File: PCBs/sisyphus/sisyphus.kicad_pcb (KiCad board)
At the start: 2 copper layers, 52 x 42 mm, 68 parts, among them J1 USB_BOOT, J10 Speaker, J2 SWD, J3 Battery, J4 USB_C_Receptacle_USB2.0_14P, J5 Keyboard, J6 AUX USB, J7 Light sensor, J8 Limit SW, J9 RGB_CONN, Q1 AO3401A, SW1 SW_SPDT_321, U1 W25Q128JVS, U2 RP2040, U3 TPS62291, U4 BQ25619, U5 USBLC6-2P6, U6 TCA8418, U7 MAX98357A, Y1 ABM8-272-T3

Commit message: Schematic refinements, start of PCB
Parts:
- removed C25: 10uF, Capacitor_SMD:C_0402_1005Metric
- removed D2: D_shottky, Diode_SMD:D_SOD-123
- removed J10: Speaker, Connector_PinHeader_2.54mm:PinHeader_1x02_P2.54mm_Vertical
- removed L2: 2.2uH 1.2A, Inductor_SMD:L_0805_2012Metric
- removed R14: DNF, Resistor_SMD:R_0402_1005Metric
- added JP2: Gain select, Jumper:SolderJumper-3_P1.3mm_Open_RoundedPad1.0x1.5mm, B.Cu at (112.5, 97.0)
- added U8: RP2040, Package_DFN_QFN:QFN-56-1EP_7x7mm_P0.4mm_EP3.2x3.2mm, F.Cu at (102.3, 95.0)
- C1: value 100nF -> 1uF
- C11, C12: value 1uF -> 100nF
- C13, C17, C20: value 10uF -> 100nF
- C14, C15: value 15pF -> 100nF
- C16: value 47nF -> 100nF
- C19: value 10uF -> 1uF
- C2, C24, C3, C7: value 100nF -> 10uF
- C22: value 4.7uF -> 15pF
- C23: value 10uF -> 15pF
- C4: value 100nF -> 0.1uF
- C5: value 100nF -> 4.7uF
- D1: value LED -> D_shottky; footprint LED_SMD:LED_0603_1608Metric -> Diode_SMD:D_SOD-123
- J1: value USB_BOOT -> Battery; footprint Connector_PinHeader_2.54mm:PinHeader_1x02_P2.54mm_Vertical -> Connector_JST:JST_PH_S3B-PH-SM4-TB_1x03-1MP_P2.00mm_Horizontal
- J2: value SWD -> USB_C_Receptacle_USB2.0_14P; footprint Connector_PinHeader_2.54mm:PinHeader_1x03_P2.54mm_Vertical -> Connector_USB:USB_C_Receptacle_G-Switch_GT-USB-7010ASV
- J3: value Battery -> USB_BOOT; footprint Connector_JST:JST_PH_S3B-PH-SM4-TB_1x03-1MP_P2.00mm_Horizontal -> Connector_PinHeader_2.54mm:PinHeader_1x02_P2.54mm_Vertical
- J4: value USB_C_Receptacle_USB2.0_14P -> SPK; footprint Connector_USB:USB_C_Receptacle_G-Switch_GT-USB-7010ASV -> Connector_JST:JST_PH_S2B-PH-SM4-TB_1x02-1MP_P2.00mm_Horizontal
- J5: value Keyboard -> RGB_CONN; footprint Connector_JST:JST_XH_S8B-XH-A_1x08_P2.50mm_Horizontal -> Connector_JST:JST_PH_S3B-PH-SM4-TB_1x03-1MP_P2.00mm_Horizontal
- J6: value AUX USB -> AUX; footprint Connector_PinHeader_2.54mm:PinHeader_1x04_P2.54mm_Vertical -> Connector_JST:JST_PH_S6B-PH-SM4-TB_1x06-1MP_P2.00mm_Horizontal
- J7: value Light sensor -> SWD; footprint Connector_JST:JST_XH_S5B-XH-A_1x05_P2.50mm_Horizontal -> Connector_PinHeader_2.54mm:PinHeader_1x03_P2.54mm_Vertical; moved to B.Cu
- J8: value Limit SW -> KEYB; footprint Connector_PinSocket_2.54mm:PinSocket_1x02_P2.54mm_Vertical -> Connector_JST:JST_PH_S8B-PH-SM4-TB_1x08-1MP_P2.00mm_Horizontal
- J9: value RGB_CONN -> PWR-BTN; footprint Connector_PinHeader_2.54mm:PinHeader_1x03_P2.54mm_Vertical -> Connector_JST:JST_PH_S2B-PH-SM4-TB_1x02-1MP_P2.00mm_Horizontal
- JP1: value Gain select -> PWR SW bypass; footprint Jumper:SolderJumper-3_P1.3mm_Open_RoundedPad1.0x1.5mm -> Jumper:SolderJumper-2_P1.3mm_Bridged2Bar_RoundedPad1.0x1.5mm; moved to B.Cu
- L1: value 1uH 2A -> 2.2uH 1.2A; footprint Inductor_SMD:L_0603_1608Metric -> Inductor_SMD:L_0805_2012Metric
- R1: value 10k -> 5.1k
- R10: value 10k -> DNF
- R11: value 10k -> 1k
- R12, R13: value 5.1k -> 10k
- R2: value 1k -> 330k
- R3: value 33 -> 5.1k
- R4: value 33 -> 7.32k
- R5: value 10k -> 100k
- R8: value 1M -> 33
- R9: value 330 -> 33
- U1: value W25Q128JVS -> TPS62291; footprint Package_SO:SOIC-8_5.23x5.23mm_P1.27mm -> Package_SON:WSON-6-1EP_2x2mm_P0.65mm_EP1x1.6mm_ThermalVias
- U2: value RP2040 -> MP2667; footprint Package_DFN_QFN:QFN-56-1EP_7x7mm_P0.4mm_EP3.2x3.2mm -> sisyphus:MPS_MP2664_QFN-10_2x2mm_P0.5mm
- U3: value TPS62291 -> USBLC6-2P6; footprint Package_SON:WSON-6-1EP_2x2mm_P0.65mm_EP1x1.6mm_ThermalVias -> Package_TO_SOT_SMD:SOT-666
- U4: value BQ25619 -> MAX17048; footprint Package_DFN_QFN:Texas_RTW_WQFN-24-1EP_4x4mm_P0.5mm_EP2.7x2.7mm_ThermalVias -> Package_DFN_QFN:TDFN-8-1EP_2x2mm_P0.5mm_EP0.8x1.2mm
- U5: value USBLC6-2P6 -> W25Q128JVP; footprint Package_TO_SOT_SMD:SOT-666 -> Package_SON:WSON-8-1EP_6x5mm_P1.27mm_EP3.4x4.3mm
- moved H4 58.2 mm to (72.0, 101.0)
- moved J7 53.7 mm to (72.9, 85.1)
- moved H2 47.4 mm to (126.0, 78.5)
- moved H1 44.4 mm to (81.0, 78.5)
- moved J6 41.9 mm to (119.5, 111.2)
- moved U5 41.5 mm to (62.4, 94.8), turned to 0 degrees
- moved H3 38.8 mm to (107.5, 113.5)
- moved R6 37.6 mm to (71.4, 90.6), turned to 0 degrees
- moved R7 32.6 mm to (71.4, 89.7), turned to 180 degrees
- moved J2 30.3 mm to (103.2, 77.8), turned to 180 degrees
- moved JP1 29.6 mm to (89.6, 82.5), turned to 0 degrees
- moved J4 28.8 mm to (124.0, 97.8), turned to 90 degrees
- moved J8 26.2 mm to (89.2, 111.2), turned to 0 degrees
- moved C8 26.0 mm to (73.4, 94.1), turned to 180 degrees
- moved R13 24.9 mm to (116.5, 105.2)
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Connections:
- C1 pad 1: +3V3 -> +5V
- C10 pad 1: +1V1 -> +3V3
- C12 pad 1: +1V1 -> +3V3
- C14 pad 1: Net-(U2-XIN) -> +3V3
- C15 pad 1: Net-(C15-Pad1) -> +3V3
- C16 pad 1: /Batery and power/SW -> +1V1
- C16 pad 2: Net-(U4-BTST) -> GND
- C17 pad 1: SYS -> +1V1
- C18 pad 1: +5V -> +3V3
- C19 pad 1: VSYS -> +1V1
- C2 pad 1: +3V3 -> /SYS
- C20 pad 1: +3V3 -> GND
- C20 pad 2: GND -> VSYS
- C21 pad 1: +BATT -> GND
- C21 pad 2: GND -> VSYS
- C22 pad 1: /Batery and power/REGN -> Net-(U8-XIN)
- C23 pad 1: GND -> Net-(C23-Pad1)
- C23 pad 2: Net-(U4-PMID) -> GND
- C24 pad 1: GND -> +3V3
- C24 pad 2: VSYS -> GND
- C3 pad 1: +3V3 -> VSYS
- C4 pad 1: +3V3 -> /CHG_VDD
- C5 pad 1: +3V3 -> +BATT
- C6 pad 1: +3V3 -> +BATT
- C9 pad 1: +1V1 -> +3V3
- D1 pad 1: Net-(D1-K) -> +5V
- D1 pad 2: Net-(D1-A) -> VBUS
- J1 pad 2: /~{USB_BOOT} -> /NTC
- J3 pad 2: /Batery and power/NTC -> /~{USB_BOOT}
- J5 pad 1: /Peripheral/ROW3 -> GND
- J5 pad 2: /Peripheral/ROW2 -> /RGB_DATA
- J5 pad 3: /Peripheral/ROW1 -> +3V3
- J6 pad 2: /Peripheral/DN -> /SDA
- J6 pad 3: /Peripheral/DP -> /SCL
- J6 pad 4: VBUS -> /AUX_LED
- J7 pad 2: SDA -> /SWD
- J7 pad 3: SCL -> /SWCLK
- J8 pad 1: GND -> /ROW3
- J8 pad 2: LMT_SW -> /ROW2
- J9 pad 1: GND -> /CHRG_INT
- J9 pad 2: RGB_DATA -> GND
- JP1 pad 1: GND -> VSYS
- JP1 pad 2: Net-(JP1-C) -> /SYS
- L1 pad 1: /Batery and power/SW -> +3V3
- L1 pad 2: SYS -> Net-(U1-SW)
- Q1 pad 2: SYS -> /SYS
- R1 pad 1: +3V3 -> GND
- R1 pad 2: /QSPI_SS -> Net-(J2-CC1)
- R10 pad 1: Net-(U4-PMID_GOOD) -> /GAIN_SELECT
- R10 pad 2: /Batery and power/REGN -> Net-(JP2-C)
- R11 pad 1: /Batery and power/REGN -> Net-(U8-XOUT)
- R11 pad 2: /Batery and power/NTC -> Net-(C23-Pad1)
- R12 pad 1: GND -> /SCL
- R12 pad 2: Net-(J4-CC1) -> +3V3
- R13 pad 1: GND -> +3V3
- R13 pad 2: Net-(J4-CC2) -> /SDA
- R2 pad 1: /QSPI_SS -> Net-(Q1-G)
- R2 pad 2: /~{USB_BOOT} -> /SYS
- R3 pad 1: USB_D+ -> GND
- R3 pad 2: Net-(U2-USB_DP) -> Net-(J2-CC2)
- R4 pad 1: USB_D- -> /CHG_VDD
- R4 pad 2: Net-(U2-USB_DM) -> /BATT_NTC
- R5 pad 1: SCL -> /CHG_VDD
- R5 pad 2: +3V3 -> /CHRG_INT
- R6 pad 2: SDA -> /QSPI_SS
- R7 pad 1: Net-(U2-XOUT) -> /QSPI_SS
- R7 pad 2: Net-(C15-Pad1) -> /~{USB_BOOT}
- R8 pad 1: Net-(Q1-G) -> /USB_D+
- R8 pad 2: SYS -> Net-(U8-USB_DP)
- R9 pad 1: Net-(D1-A) -> /USB_D-
- R9 pad 2: SYS -> Net-(U8-USB_DM)
- U1 pad 1: /QSPI_SS -> Net-(U1-SW)
- U1 pad 2: /QSPI_SD1 -> GND
- U1 pad 3: /QSPI_SD2 -> +3V3
- U1 pad 4: GND -> VSYS
- U1 pad 5: /QSPI_SD0 -> VSYS
- U1 pad 6: /QSPI_SCLK -> GND
- U1 pad 7: /QSPI_SD3 -> GND
- U2 pad 1: +3V3 -> +5V
- U2 pad 10: +3V3 -> /SYS
- U2 pad 2: unconnected-(U2-GPIO0-Pad2) -> /BATT_NTC
- U2 pad 3: unconnected-(U2-GPIO1-Pad3) -> /CHRG_INT
- U2 pad 4: unconnected-(U2-GPIO2-Pad4) -> /CHG_VDD
- U2 pad 5: unconnected-(U2-GPIO3-Pad5) -> GND
- U2 pad 6: unconnected-(U2-GPIO4-Pad6) -> /SCL
- U2 pad 7: unconnected-(U2-GPIO5-Pad7) -> /SDA
- U2 pad 8: unconnected-(U2-GPIO6-Pad8) -> +BATT
- U2 pad 9: unconnected-(U2-GPIO7-Pad9) -> +BATT
- U3 pad 1: Net-(U3-SW) -> /DN
- U3 pad 3: +3V3 -> /DP
- U3 pad 4: VSYS -> /USB_D+
- U3 pad 5: VSYS -> VBUS
- U3 pad 6: GND -> /USB_D-
- U4 pad 1: +5V -> GND
- U4 pad 2: unconnected-(U4-PSEL-Pad2) -> +BATT
- U4 pad 3: Net-(U4-PMID_GOOD) -> +BATT
- U4 pad 4: Net-(D1-K) -> GND
- U4 pad 5: SCL -> /GAUGE_INT
- U4 pad 6: SDA -> GND
- U4 pad 7: PMIC_INT -> /SCL
- U4 pad 8: unconnected-(U4-NC-Pad8) -> /SDA
- U5 pad 1: /Peripheral/DN -> /QSPI_SS
- U5 pad 2: GND -> /QSPI_SD1
- U5 pad 3: /Peripheral/DP -> /QSPI_SD2
- U5 pad 4: USB_D+ -> GND
- U5 pad 5: +5V -> /QSPI_SD0
- U5 pad 6: USB_D- -> /QSPI_SCLK
- U6 pad 10: /Peripheral/COL1 -> /COL1
- U6 pad 11: /Peripheral/COL2 -> /COL2
- U6 pad 12: /Peripheral/COL3 -> /COL3
- U6 pad 20: KEYPAD_RESET -> /KEYPAD_RESET
- U6 pad 22: SDA -> /SDA
- U6 pad 23: SCL -> /SCL
- U6 pad 24: KEYPAD_INT -> /KEYPAD_INT
- U6 pad 5: /Peripheral/ROW3 -> /ROW3
- U6 pad 6: /Peripheral/ROW2 -> /ROW2
- U6 pad 7: /Peripheral/ROW1 -> /ROW1
- U6 pad 8: /Peripheral/ROW0 -> /ROW0
- U6 pad 9: /Peripheral/COL0 -> /COL0
- U7 pad 1: I2S_DATA -> /I2S_DATA
- U7 pad 10: /Peripheral/SPK- -> /SPK-
- U7 pad 14: I2S_FRAME_CLOCK -> /I2S_FRAME_CLOCK
- U7 pad 16: I2S_BIT_CLOCK -> /I2S_BIT_CLOCK
- U7 pad 2: /Peripheral/GAIN_SELECT -> /GAIN_SELECT
- U7 pad 4: I2S_ENABLE -> /I2S_ENABLE
- U7 pad 9: /Peripheral/SPK+ -> /SPK+
- Y1 pad 1: Net-(U2-XIN) -> Net-(U8-XIN)
- Y1 pad 3: Net-(C15-Pad1) -> Net-(C23-Pad1)
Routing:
- net +3V3: track 133.1 -> 23.9 mm, vias 14 -> 0
- net SCL: track 46.1 -> 0.00 mm, vias 6 -> 0
- net SDA: track 46.0 -> 0.00 mm, vias 3 -> 0
- net GND: track 57.2 -> 20.0 mm, vias 61 -> 5
- net /QSPI_SS: track 21.3 -> 0.00 mm
- net PMIC_INT: track 20.6 -> 0.00 mm, vias 4 -> 0
- net AUX_LED: track 18.8 -> 0.00 mm
- net VSYS: track 23.9 -> 5.32 mm, vias 5 -> 0
- net /Peripheral/DP: track 17.9 -> 0.00 mm
- net /Peripheral/DN: track 17.8 -> 0.00 mm
- net /Batery and power/REGN: track 16.0 -> 0.00 mm, vias 3 -> 0
- net /QSPI_SD1: track 14.8 -> 0.00 mm
- net Net-(D1-K): track 14.4 -> 0.00 mm, vias 2 -> 0
- net Net-(Q1-G): track 13.1 -> 0.00 mm, vias 1 -> 0
- net /Batery and power/NTC: track 12.7 -> 0.00 mm
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- removed copper zone on F.Cu, net +5V
- removed copper zone on F.Cu, net SYS
- removed copper zone on B.Cu, net VSYS
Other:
- board size 52 x 42 mm -> 51.5 x 41.5 mm
- board text added: "U2"
- board text removed: "+"
- board text removed: "-"
- board text removed: "AUX USB"
- board text removed: "Ano, prosím"
- board text removed: "BAT"
- board text removed: "BOOT"
- board text removed: "CLANG!"
- board text removed: "GAIN SLCT"
- board text removed: "I2C CLR SENS"
- board text removed: "Ještě víc!"
- board text removed: "KBD"
- board text removed: "LMT SW"
- board text removed: "Made with by Plajta"
- board text removed: "NTC"
- board text removed: "ON"
- board text removed: "RGB LED"
- board text removed: "SPK"
- board text removed: "SWD"
- board text removed: "SisyFOSS"
- board text removed: "β"

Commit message: PCB tweaks
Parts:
- moved J7 48.4 mm to (120.8, 78.0)
- moved R7 43.5 mm to (113.7, 79.5)
- moved R6 43.5 mm to (113.7, 80.4)
- moved U5 35.3 mm to (97.0, 87.8)
- moved J8 30.3 mm to (119.4, 108.4)
- moved C8 29.1 mm to (101.4, 86.3), turned to -90 degrees
- moved C24 27.1 mm to (98.0, 102.8)
- moved J6 27.1 mm to (92.5, 108.4)
- moved R12 27.1 mm to (91.5, 102.3)
- moved R13 27.1 mm to (89.5, 102.3)
- moved U6 22.6 mm to (114.0, 100.6), turned to 90 degrees
- moved H4 12.4 mm to (80.0, 110.5)
- moved J3 7.63 mm to (111.2, 80.0)
- moved H3 3.91 mm to (105.0, 110.5)
- moved C4 3.71 mm to (89.5, 83.0)
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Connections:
- J1 pad 2: /NTC -> /BATT_NTC
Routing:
- net /QSPI_SS: track 0.00 -> 12.3 mm
- net /QSPI_SD1: track 0.00 -> 11.1 mm
- net /KEYPAD_INT: track 10.9 -> 0.00 mm
- net /QSPI_SD2: track 0.00 -> 9.70 mm
- net /KEYPAD_RESET: track 9.57 -> 0.00 mm
- net +1V1: track 6.82 -> 16.2 mm, vias 2 -> 4
- net /BATT_NTC: track 1.00 -> 10.1 mm, vias 0 -> 2
- net /COL3: track 5.69 -> 14.6 mm
- net /COL2: track 3.85 -> 12.4 mm
- net +3V3: track 23.9 -> 30.9 mm
- net /COL1: track 3.23 -> 9.45 mm
- net /QSPI_SD3: track 0.00 -> 5.02 mm
- net /ROW3: track 9.79 -> 4.82 mm
- net /ROW2: track 7.99 -> 3.35 mm
- net GND: track 20.0 -> 24.3 mm, vias 5 -> 8
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- removed copper zone on F.Cu, net +BATT
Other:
- board size 51.5 x 41.5 mm -> 53.5 x 38.5 mm

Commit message: PCB roated, far from perfect
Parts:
- added REF**: Panasonic_EVQPUL_EVQPUC, Button_Switch_SMD:Panasonic_EVQPUL_EVQPUC, F.Cu at (122.8, 70.1)
- moved JP2 9.75 mm to (120.2, 87.2), turned to 180 degrees
- moved R10 7.69 mm to (119.0, 88.9), turned to 0 degrees
- moved JP1 7.62 mm to (94.2, 83.2), turned to 90 degrees
- moved C21 7.12 mm to (114.9, 91.7), turned to 0 degrees
- moved C20 6.74 mm to (114.9, 92.7), turned to 0 degrees
- moved R5 6.05 mm to (87.0, 80.2), turned to -90 degrees
- moved C1 5.85 mm to (89.8, 81.2), turned to 90 degrees
- moved R4 5.75 mm to (88.8, 80.2), turned to -90 degrees
- moved C3 5.39 mm to (110.0, 81.0), turned to 180 degrees
- moved C4 4.47 mm to (85.5, 81.0)
- moved C2 3.78 mm to (90.2, 83.2)
- moved Q1 3.72 mm to (92.8, 83.8), turned to -90 degrees
- moved J3 3.64 mm to (113.3, 77.0), turned to -90 degrees
- moved U7 3.57 mm to (118.0, 91.5), turned to -90 degrees
- moved U4 2.92 mm to (88.8, 92.0), turned to -90 degrees
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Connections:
- U8 pad 15: /KEYPAD_INT -> /LMT_SW
- U8 pad 16: /KEYPAD_RESET -> /AUX_LED
- U8 pad 30: /LMT_SW -> /KEYPAD_INT
- U8 pad 31: /AUX_LED -> /KEYPAD_RESET
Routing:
- net /SDA: track 0.00 -> 65.4 mm, vias 0 -> 6
- net /CHRG_INT: track 1.99 -> 66.9 mm, vias 1 -> 4
- net /SCL: track 0.00 -> 64.2 mm, vias 0 -> 6
- net +3V3: track 30.9 -> 93.8 mm, vias 0 -> 6
- net VSYS: track 5.32 -> 47.0 mm, vias 0 -> 3
- net /SWD: track 2.13 -> 33.5 mm
- net /SWCLK: track 2.91 -> 33.4 mm
- net /QSPI_SS: track 12.3 -> 39.5 mm, vias 0 -> 2
- net /I2S_BIT_CLOCK: track 0.00 -> 18.0 mm, vias 0 -> 2
- net /I2S_FRAME_CLOCK: track 0.00 -> 17.7 mm, vias 0 -> 2
- net /AUX_LED: track 0.00 -> 17.1 mm
- net /I2S_DATA: track 0.00 -> 16.9 mm, vias 0 -> 2
- net /GAUGE_INT: track 0.00 -> 15.6 mm, vias 0 -> 2
- net /I2S_ENABLE: track 0.00 -> 15.0 mm, vias 0 -> 2
- net /RGB_DATA: track 0.00 -> 14.9 mm
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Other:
- board size 53.5 x 38.5 mm -> 51.5 x 38.5 mm

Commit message: Add GND return paths, move USB_BOOT
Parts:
- J3: footprint Connector_PinHeader_2.54mm:PinHeader_1x02_P2.54mm_Vertical -> Connector_PinHeader_1.00mm:PinHeader_1x02_P1.00mm_Vertical
- moved J3 24.1 mm to (94.4, 92.0)
- moved R7 20.2 mm to (93.0, 86.3)
- moved R6 18.9 mm to (95.8, 84.5)
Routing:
- net /QSPI_SS: track 39.5 -> 14.7 mm, vias 2 -> 0
- net +3V3: track 93.8 -> 88.5 mm, vias 6 -> 5
- net /~{USB_BOOT}: track 2.71 -> 6.08 mm
- net GND: track 37.4 -> 37.2 mm, vias 7 -> 31

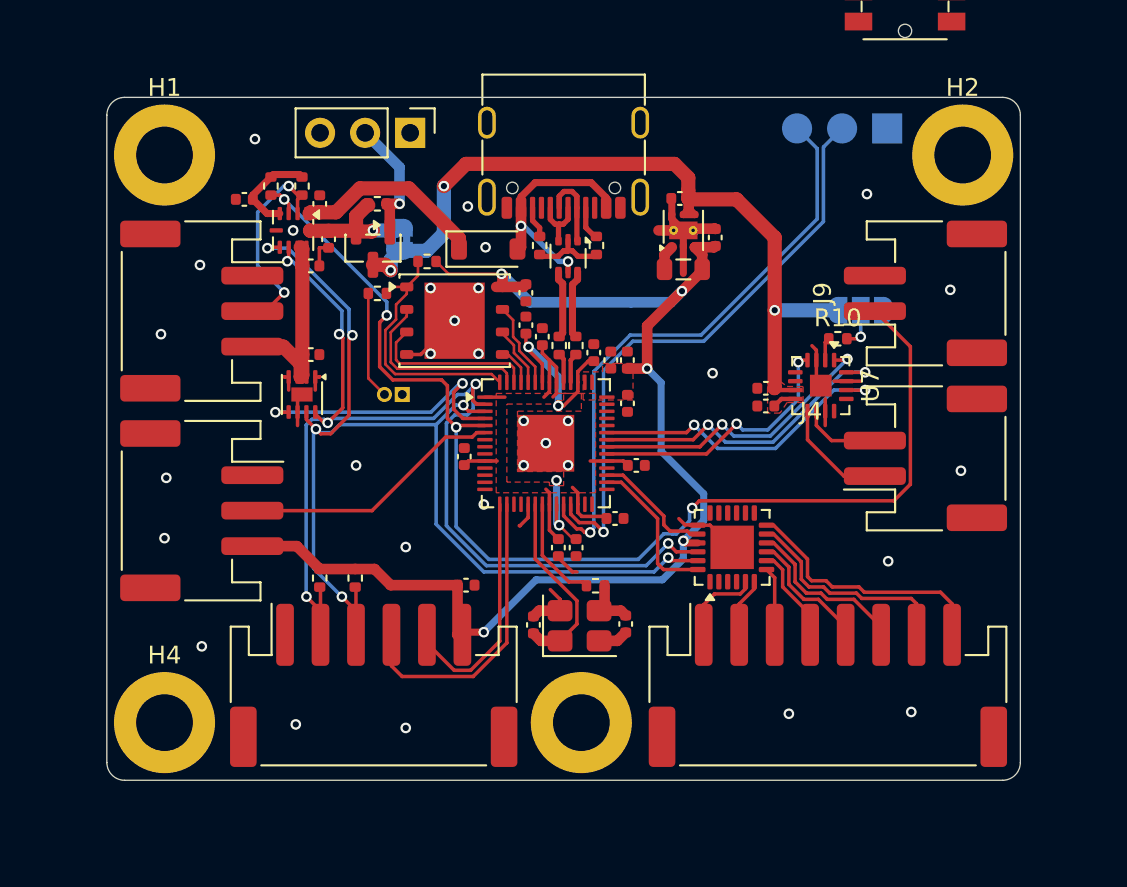
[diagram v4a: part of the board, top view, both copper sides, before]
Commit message: PCB smaller now
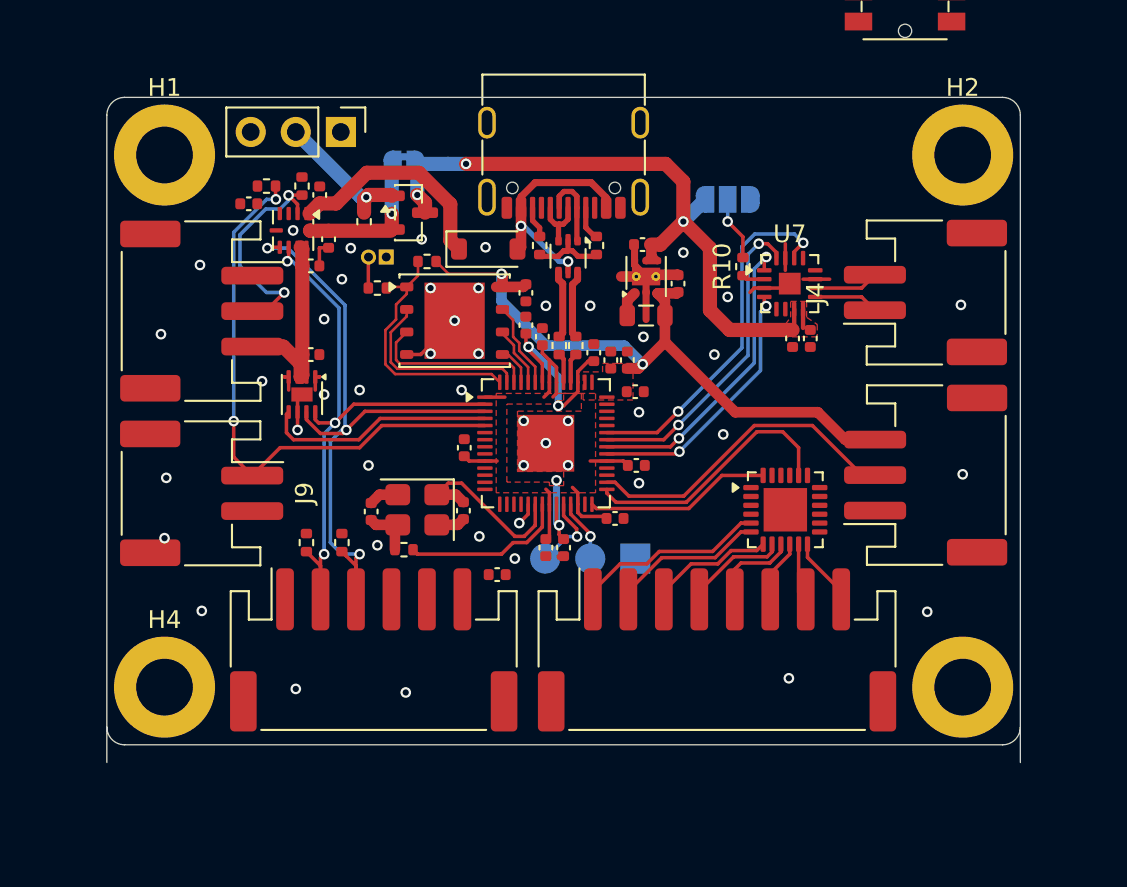
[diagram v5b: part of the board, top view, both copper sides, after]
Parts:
- moved J9 42.3 mm to (83.1, 97.6), turned to -90 degrees
- moved J5 40.9 mm to (123.9, 96.5), turned to 90 degrees
- moved J7 28.1 mm to (107.5, 101.2)
- moved H3 21.6 mm to (126.0, 108.5)
- moved C23 15.7 mm to (92.7, 98.6), turned to 90 degrees
- moved Y1 11.2 mm to (95.2, 98.5), turned to 180 degrees
- moved R11 11.0 mm to (94.5, 100.8), turned to 180 degrees
- moved JP2 9.76 mm to (112.8, 81.0)
- moved J4 9.35 mm to (123.9, 86.2)
- moved J3 7.80 mm to (93.5, 84.2)
- moved C22 7.55 mm to (97.8, 98.5), turned to -90 degrees
- moved R10 6.72 mm to (113.6, 84.8), turned to 90 degrees
- moved J8 6.56 mm to (112.2, 106.4)
- moved U7 6.01 mm to (116.2, 85.8), turned to 0 degrees
- moved C20 4.56 mm to (117.4, 88.8), turned to 90 degrees
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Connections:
- U8 pad 28: unconnected-(U8-GPIO17-Pad28) -> /KEYPAD_INT
- U8 pad 29: unconnected-(U8-GPIO18-Pad29) -> /KEYPAD_RESET
- U8 pad 30: /KEYPAD_INT -> /RGB_DATA
- U8 pad 31: /KEYPAD_RESET -> unconnected-(U8-GPIO20-Pad31)
- U8 pad 6: /RGB_DATA -> unconnected-(U8-GPIO4-Pad6)
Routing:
- net /CHRG_INT: track 66.9 -> 32.3 mm, vias 4 -> 2
- net +3V3: track 88.5 -> 55.5 mm, vias 5 -> 2
- net /SDA: track 65.4 -> 35.2 mm, vias 6 -> 3
- net /SWD: track 33.5 -> 3.53 mm
- net /SWCLK: track 33.4 -> 4.45 mm
- net /SCL: track 64.2 -> 39.3 mm, vias 6 -> 3
- net /AUX_LED: track 17.1 -> 0.00 mm
- net /LMT_SW: track 13.6 -> 0.00 mm
- net /COL3: track 14.6 -> 3.90 mm
- net /COL2: track 12.4 -> 3.28 mm
- net /KEYPAD_RESET: track 6.79 -> 14.8 mm
- net VSYS: track 47.0 -> 40.5 mm
- net GND: track 37.2 -> 30.8 mm, vias 31 -> 46
- net /ROW3: track 4.82 -> 11.0 mm
- net /COL1: track 9.45 -> 3.57 mm
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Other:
- board size 51.5 x 38.5 mm -> 51.5 x 37.5 mm

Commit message: PCB Hopefuly done
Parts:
- removed REF**: Panasonic_EVQPUL_EVQPUC, Button_Switch_SMD:Panasonic_EVQPUL_EVQPUC
- moved C12 0.72 mm to (97.4, 95.5), turned to 180 degrees
- moved R12 0.61 mm to (90.5, 100.0)
- moved R13 0.61 mm to (89.5, 100.0)
- moved R2 0.50 mm to (91.8, 82.2)
- moved C1 0.50 mm to (89.8, 81.2)
- moved Q1 0.50 mm to (94.2, 81.8)
- moved JP1 0.25 mm to (94.5, 79.2)
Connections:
- U8 pad 15: /LMT_SW -> unconnected-(U8-GPIO12-Pad15)
- U8 pad 16: /AUX_LED -> unconnected-(U8-GPIO13-Pad16)
- U8 pad 6: unconnected-(U8-GPIO4-Pad6) -> /LMT_SW
- U8 pad 7: unconnected-(U8-GPIO5-Pad7) -> /AUX_LED
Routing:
- net +3V3: track 55.5 -> 113.8 mm, vias 2 -> 5
- net /SDA: track 35.2 -> 71.3 mm, vias 3 -> 4
- net /SCL: track 39.3 -> 72.5 mm, vias 3 -> 4
- net VSYS: track 40.5 -> 14.6 mm, vias 3 -> 7
- net /LMT_SW: track 0.00 -> 21.7 mm, vias 0 -> 2
- net /AUX_LED: track 0.00 -> 20.0 mm, vias 0 -> 2
- net /CHG_VDD: track 0.00 -> 5.55 mm
- net GND: track 30.8 -> 35.2 mm, vias 46 -> 67
- net /CHRG_INT: track 32.3 -> 33.6 mm
- net /SYS: track 8.27 -> 8.95 mm
- net /BATT_NTC: track 12.9 -> 13.6 mm
- net Net-(Q1-G): track 7.93 -> 8.51 mm
- added copper zone on B.Cu, net VSYS
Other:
- board size 51.5 x 37.5 mm -> 51.5 x 36.5 mm

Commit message: PCB Small tweaks
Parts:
- moved J7 0.50 mm to (107.5, 101.8)
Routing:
- net GND: track 35.2 -> 38.1 mm, vias 67 -> 73
- net /SWD: track 3.53 -> 4.53 mm
- net /BATT_NTC: track 13.6 -> 14.2 mm
- net +3V3: track 113.8 -> 114.4 mm
- net +1V1: track 15.6 -> 16.1 mm
- net /SYS: track 8.95 -> 9.45 mm

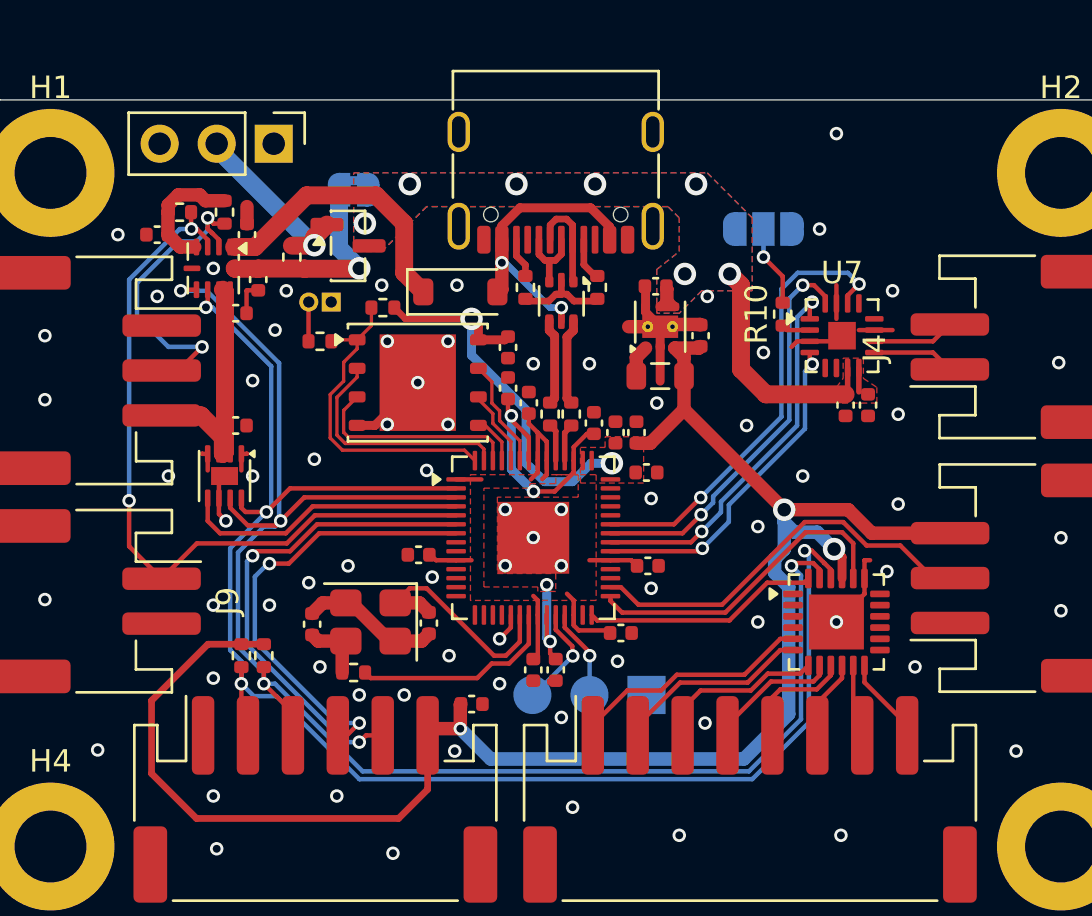
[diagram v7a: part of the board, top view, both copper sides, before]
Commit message: Repaired Crystal and pushed RP2040 north
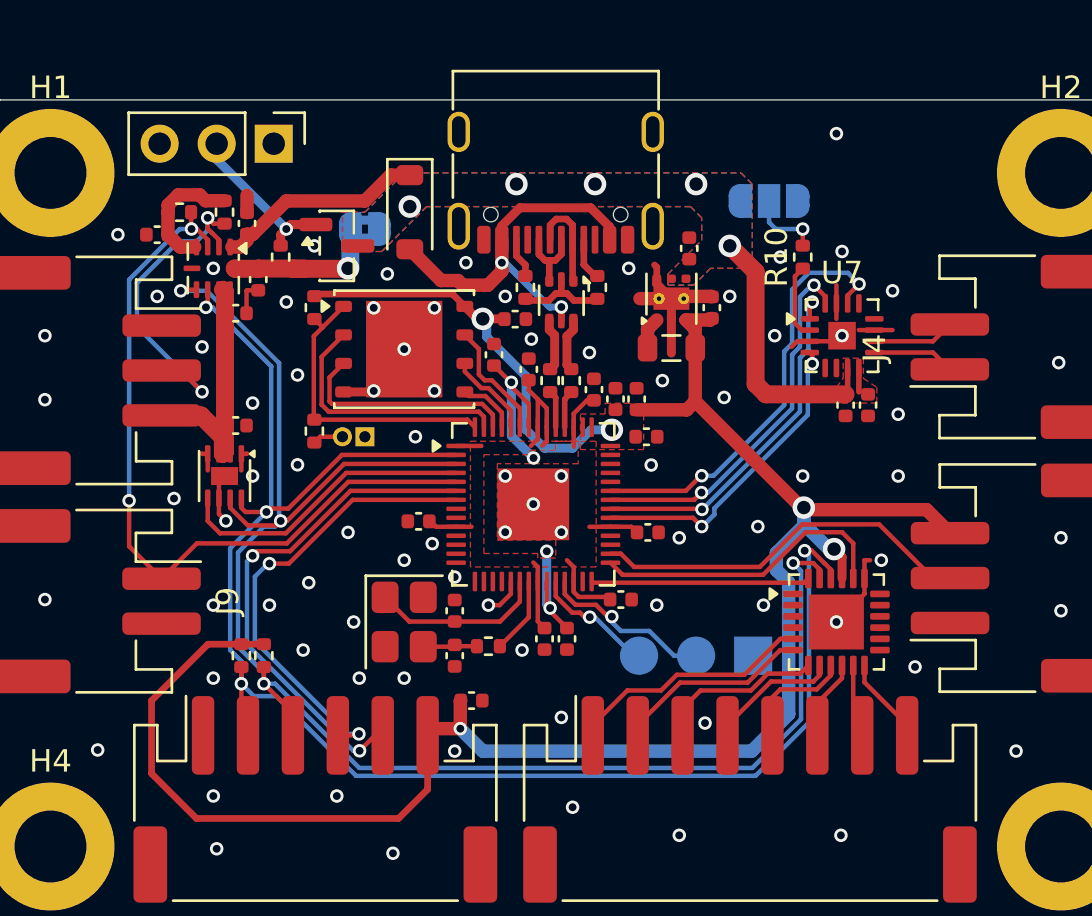
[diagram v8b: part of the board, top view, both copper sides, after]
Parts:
- moved C23 6.50 mm to (99.0, 100.0), turned to -90 degrees
- moved J3 6.18 mm to (95.0, 90.2)
- moved R11 6.11 mm to (100.5, 99.6)
- moved J7 5.06 mm to (112.3, 100.0)
- moved D1 4.20 mm to (97.0, 80.2), turned to -90 degrees
- moved R7 4.01 mm to (92.8, 90.0), turned to -90 degrees
- moved R6 3.05 mm to (92.8, 84.5), turned to -90 degrees
- moved R10 2.69 mm to (114.5, 82.2)
- moved C3 2.26 mm to (109.4, 81.9), turned to 90 degrees
- moved JP1 1.82 mm to (95.0, 81.0)
- moved C16 1.62 mm to (100.8, 86.6)
- moved U5 1.61 mm to (96.8, 86.3)
- moved C13 1.59 mm to (107.5, 90.2)
- moved Y1 1.50 mm to (96.8, 98.5), turned to -90 degrees
- moved C18 1.49 mm to (106.2, 88.6)
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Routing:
- net GND: track 38.1 -> 29.9 mm, vias 73 -> 81
- net Net-(U8-XOUT): track 9.31 -> 3.41 mm
- net VBUS: track 13.2 -> 17.2 mm
- net /SWD: track 4.53 -> 7.69 mm
- net +5V: track 12.4 -> 9.41 mm
- net Net-(U8-XIN): track 10.2 -> 7.71 mm
- net /SYS: track 9.45 -> 7.37 mm
- net /GAIN_SELECT: track 1.30 -> 3.38 mm
- net VSYS: track 14.6 -> 13.0 mm, vias 7 -> 5
- net /USB_D-: track 3.88 -> 2.42 mm
- net /USB_D+: track 3.86 -> 2.40 mm
- net +3V3: track 114.4 -> 115.8 mm
- net /I2S_BIT_CLOCK: track 18.0 -> 16.7 mm
- net +1V1: track 16.1 -> 14.9 mm
- net Net-(Q1-G): track 8.51 -> 7.32 mm
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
